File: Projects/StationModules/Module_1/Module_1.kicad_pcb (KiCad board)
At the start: 2 copper layers, 120 parts, among them J2 +310, J3 -310, J4 PowerTrans1, J5 PowerTrans2, M1 BluePillStm32, Q1 STD20NF06T4, Q2 STD20NF06T4, Q3 STD20NF06T4, Q4 STD20NF06T4, Q5 IRGB10B60KD, Q6 IRGB10B60KD, Q7 IRGB10B60KD, Q8 IRGB10B60KD, T1 Transformer_SP_2S, T2 Transformer_SP_2S, U1 PC817, U2 L7805, U3 TC1047AxNB, U5 LM311, U6 6N137

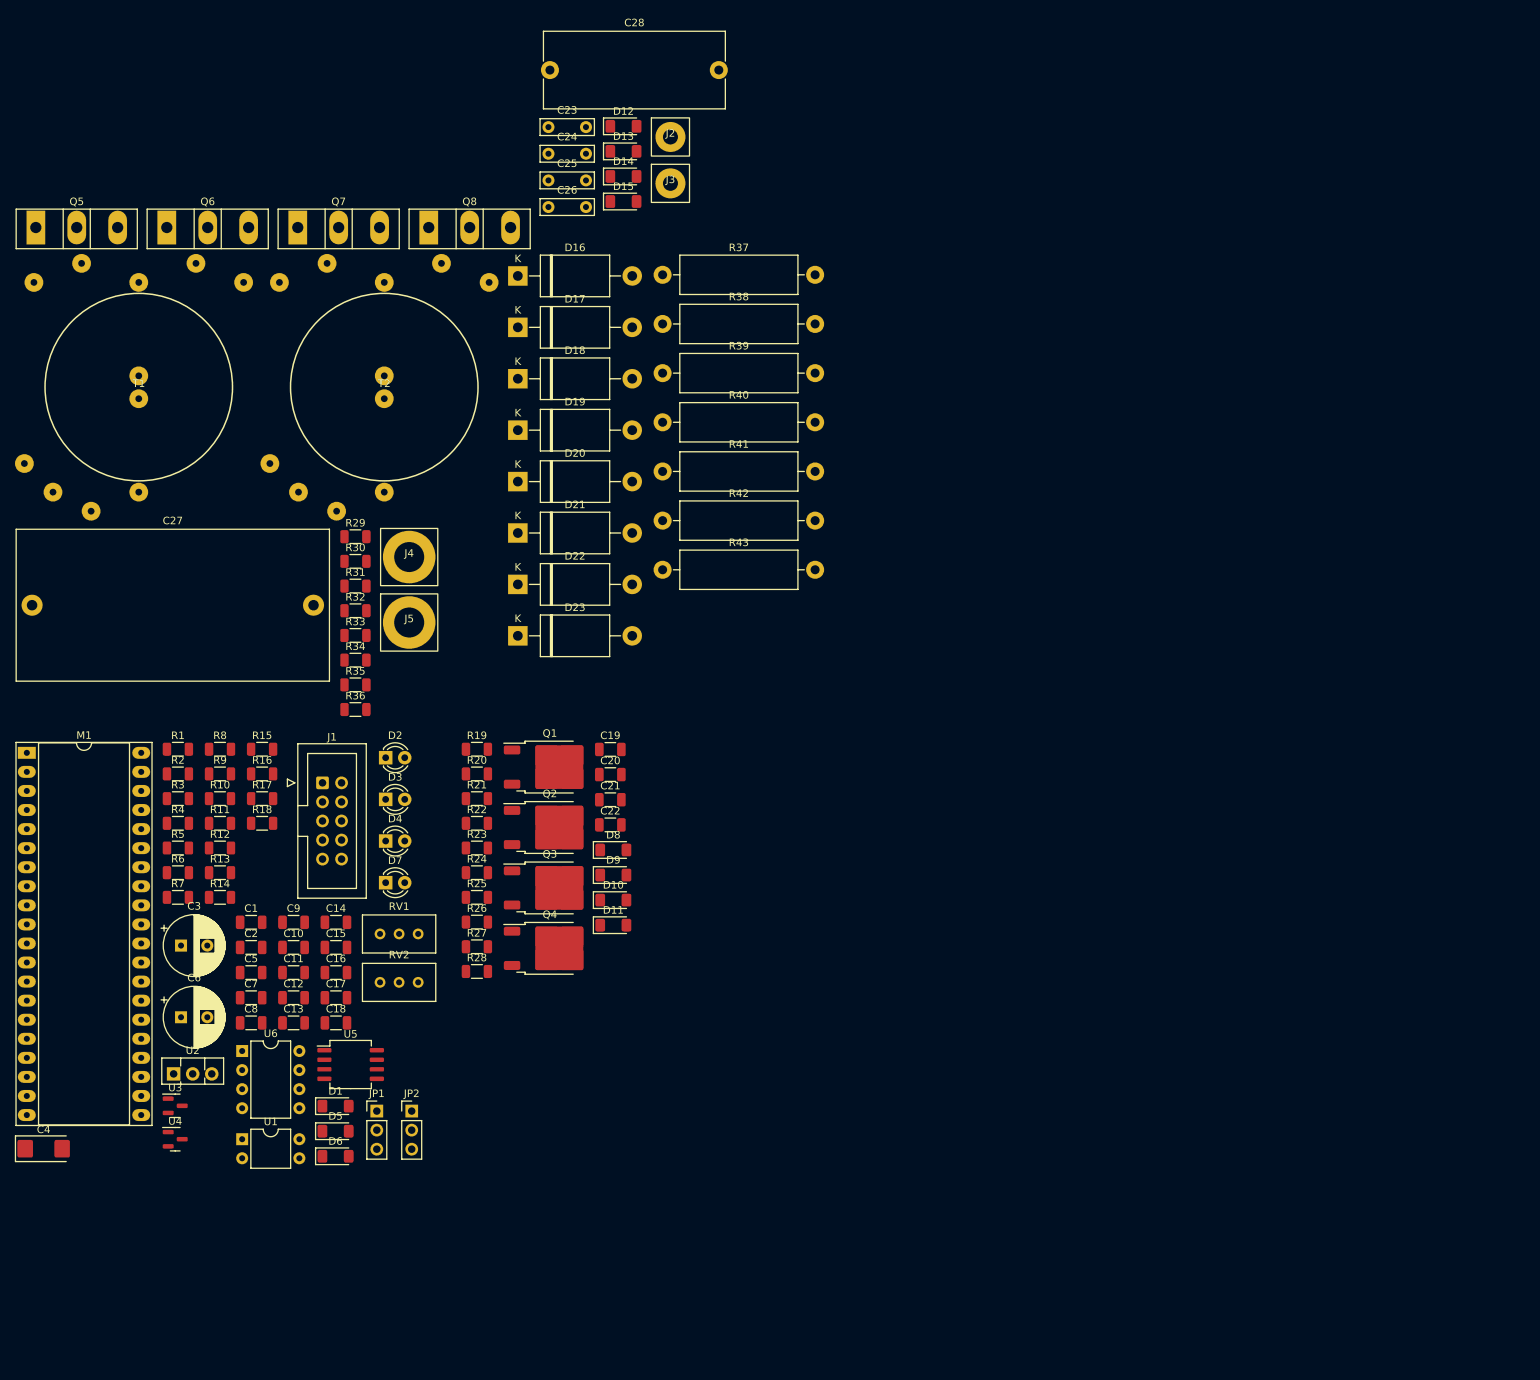
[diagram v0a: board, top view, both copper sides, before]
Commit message: Place elements 1
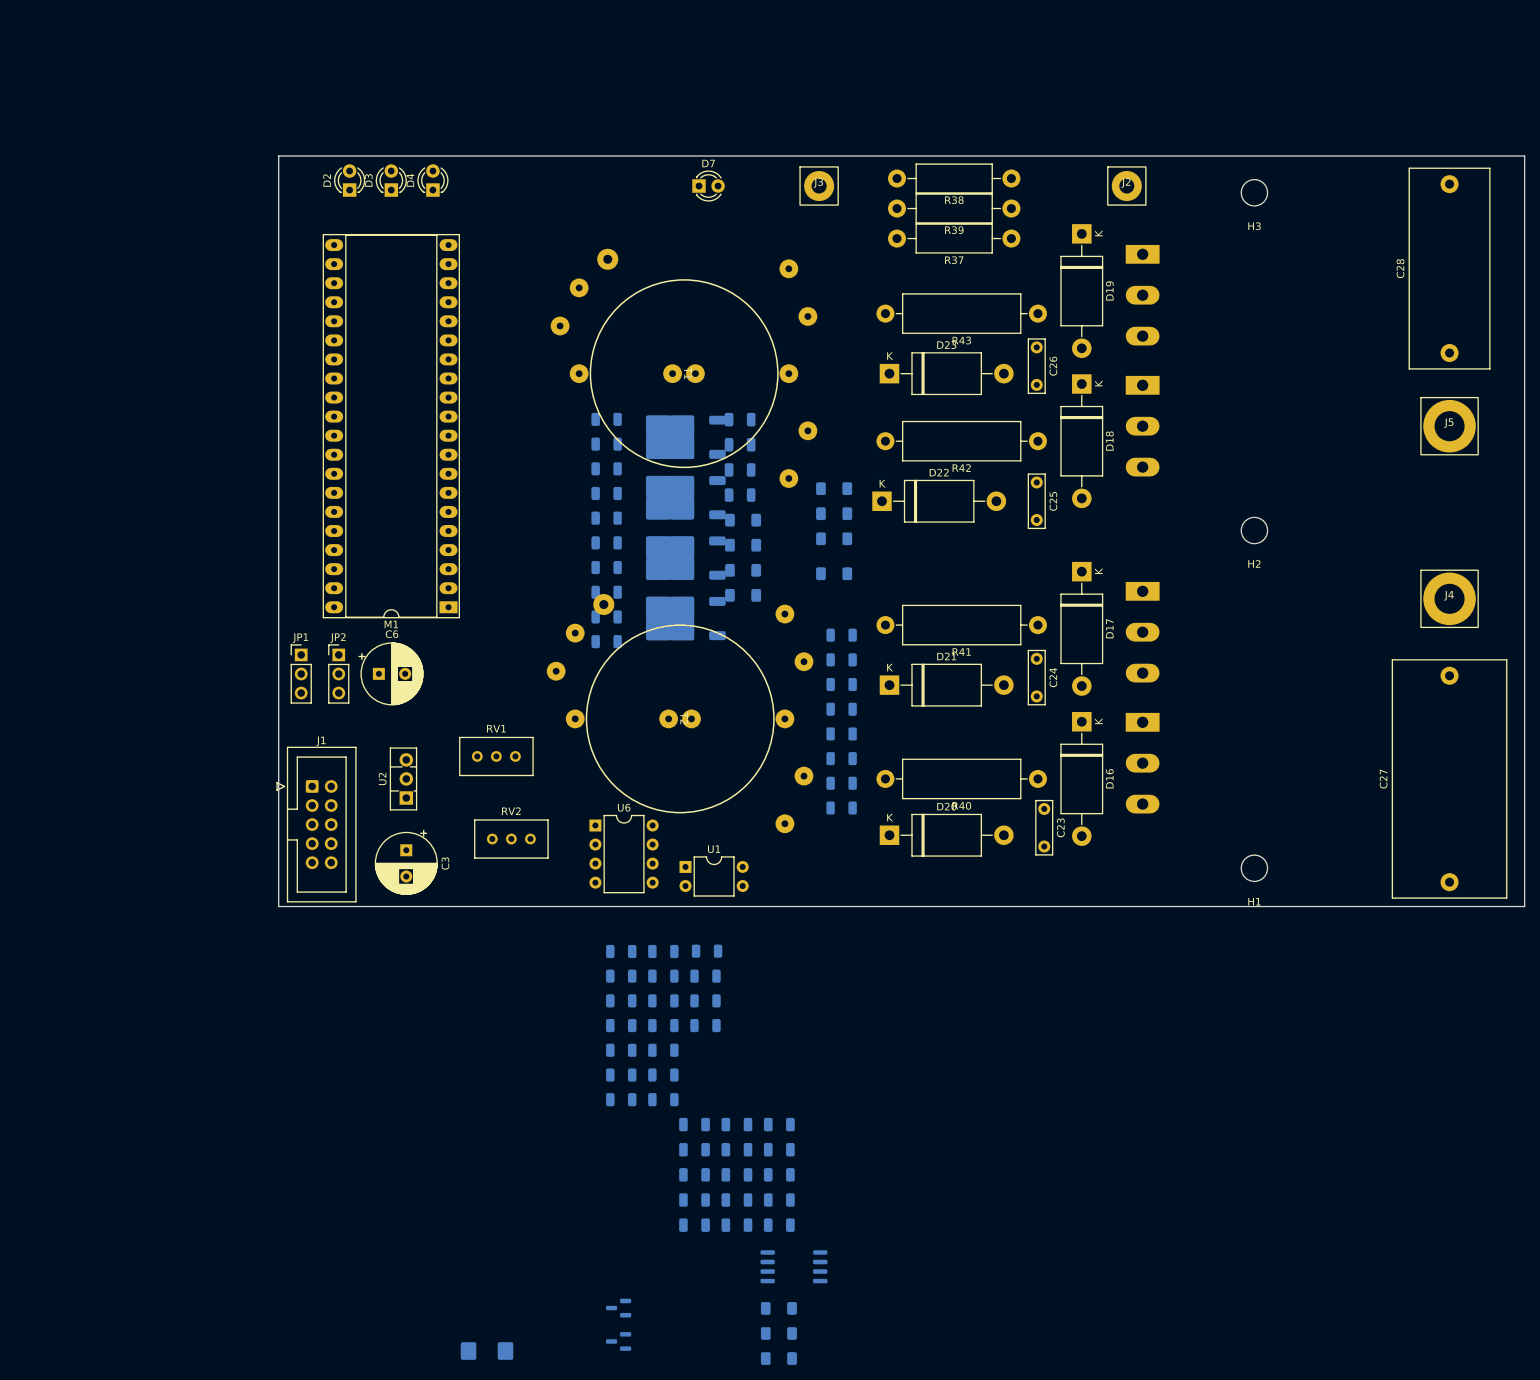
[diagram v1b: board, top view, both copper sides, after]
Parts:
- added H1: MountingHole, MountingHole:MountingHole_3.5mm, F.Cu at (184.0, 130.9)
- added H2: MountingHole, MountingHole:MountingHole_3.5mm, F.Cu at (184.0, 85.9)
- added H3: MountingHole, MountingHole:MountingHole_3.5mm, F.Cu at (184.0, 40.9)
- C1, C10, C11, C12, C13, C14, C15, C16, C17, C18, C19, C2, C20, C21, C22, C4, C5, C7, C8, C9, D1, D10, D11, D12, D13, D14, D15, D5, D6, D8, D9, Q1, Q2, Q3, Q4, R1, R10, R11, R12, R13, R14, R15, R16, R17, R18, R19, R2, R20, R21, R22, R23, R24, R25, R26, R27, R28, R29, R3, R30, R31, R32, R33, R34, R35, R36, R4, R5, R6, R7, R8, R9, U3, U4, U5: moved to B.Cu
- C27: footprint Capacitor_THT:C_Rect_L41.5mm_W20.0mm_P37.50mm_MKS4 -> Capacitor_THT:C_Rect_L31.5mm_W15.0mm_P27.50mm_MKS4
- C28: footprint Capacitor_THT:C_Rect_L24.0mm_W10.1mm_P22.50mm_MKT -> Capacitor_THT:C_Rect_L26.5mm_W10.5mm_P22.50mm_MKS4
- Q5, Q6, Q7, Q8: footprint Package_TO_SOT_THT:TO-247-3_Vertical -> Z_Package_TO:TO-247-3_Horizontal_TabUp; moved to B.Cu
- R37, R38, R39: footprint Resistor_THT:R_Axial_DIN0516_L15.5mm_D5.0mm_P20.32mm_Horizontal -> Resistor_THT:R_Axial_DIN0411_L9.9mm_D3.6mm_P15.24mm_Horizontal
- moved C27 192.4 mm to (210.0, 132.8), turned to 90 degrees
- moved Q5 161.5 mm to (169.1, 111.5), turned to -90 degrees
- moved J5 141.1 mm to (210.0, 72.0)
- moved Q6 138.8 mm to (169.1, 94.0), turned to -90 degrees
- moved J4 138.7 mm to (210.0, 95.0)
- moved C28 125.6 mm to (210.0, 62.2), turned to 90 degrees
- moved Q7 114.5 mm to (169.1, 66.5), turned to -90 degrees
- moved C23 112.3 mm to (156.0, 123.0), turned to -90 degrees
- moved D7 101.8 mm to (110.0, 40.0)
- moved D16 95.8 mm to (161.0, 111.4), turned to -90 degrees
- moved Q8 95.2 mm to (169.1, 49.1), turned to -90 degrees
- moved C24 93.6 mm to (155.0, 103.0), turned to -90 degrees
- moved D4 87.0 mm to (74.5, 40.5), turned to 90 degrees
- moved D17 81.9 mm to (161.0, 91.4), turned to -90 degrees
- moved D3 81.2 mm to (69.0, 40.5), turned to 90 degrees
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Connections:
- C24 pad 1: Net-(D16-A1) -> Net-(D16-A2)
- C26 pad 1: Net-(D18-A1) -> Net-(D18-A2)
- C27 pad 1: Net-(D16-A1) -> Net-(D16-A2)
- D16 pad 1: Net-(D16-A1) -> Net-(D14-A)
- D16 pad 2: Net-(D14-A) -> Net-(D16-A2)
- D17 pad 1: /Shunt+ -> Net-(D15-A)
- D17 pad 2: Net-(D15-A) -> /Shunt+
- D18 pad 1: Net-(D18-A1) -> Net-(D12-A)
- D18 pad 2: Net-(D12-A) -> Net-(D18-A2)
- D19 pad 1: /Shunt+ -> Net-(D13-A)
- D19 pad 2: Net-(D13-A) -> /Shunt+
- D20 pad 1: Net-(D16-A1) -> Net-(D16-A2)
- D22 pad 1: Net-(D18-A1) -> Net-(D18-A2)
- J5 pad 1: Net-(D18-A1) -> Net-(D18-A2)
- Q5 pad 3: Net-(D16-A1) -> Net-(D16-A2)
- Q6 pad 2: Net-(D16-A1) -> Net-(D16-A2)
- Q7 pad 3: Net-(D18-A1) -> Net-(D18-A2)
- Q8 pad 2: Net-(D18-A1) -> Net-(D18-A2)
- R33 pad 1: Net-(D16-A1) -> Net-(D16-A2)
- R35 pad 1: Net-(D18-A1) -> Net-(D18-A2)
- R40 pad 2: Net-(D16-A1) -> Net-(D16-A2)
- R42 pad 2: Net-(D18-A1) -> Net-(D18-A2)
- T1 pad 5: Net-(D16-A1) -> Net-(D16-A2)
- T2 pad 5: Net-(D18-A1) -> Net-(D18-A2)
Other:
- board outline added: 166 x 100 mm

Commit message: Place elements 2
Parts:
- moved U3 152.5 mm to (162.6, 50.8)
- moved C12 136.0 mm to (162.6, 47.6), turned to 0 degrees
- moved R7 125.6 mm to (78.5, 37.9), turned to 0 degrees
- moved C1 122.8 mm to (78.5, 46.2)
- moved C2 121.2 mm to (78.5, 51.2)
- moved R6 120.1 mm to (78.5, 40.2), turned to 0 degrees
- moved R5 114.9 mm to (78.5, 42.2), turned to 0 degrees
- moved C4 109.1 mm to (103.5, 88.3), turned to 90 degrees
- moved R9 107.8 mm to (162.6, 54.0)
- moved C11 101.4 mm to (73.7, 79.2), turned to 0 degrees
- moved D1 95.4 mm to (82.5, 102.0), turned to -90 degrees
- moved D7 95.0 mm to (123.8, 134.0), turned to 90 degrees
- moved J3 93.6 mm to (137.0, 133.0)
- moved C10 90.4 mm to (73.7, 88.1), turned to 0 degrees
- moved R37 87.7 mm to (163.0, 134.0)
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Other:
- board size 166 x 100 mm -> 155 x 100 mm

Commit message: Trace complit 1
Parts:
- added ?: , , F.Cu at (206.0, 41.7)
- added C29: 0,1uF, Capacitor_SMD:C_1206_3216Metric, B.Cu at (151.6, 39.9)
- moved C19 42.1 mm to (105.9, 44.2)
- moved D2 38.8 mm to (64.0, 72.4), turned to -90 degrees
- moved D3 35.4 mm to (64.0, 63.0), turned to -90 degrees
- moved D4 35.1 mm to (64.0, 53.3), turned to -90 degrees
- moved R27 30.0 mm to (117.6, 54.6), turned to 90 degrees
- moved R5 30.0 mm to (65.0, 68.9), turned to -90 degrees
- moved J2 28.0 mm to (157.0, 85.3)
- moved D8 27.9 mm to (102.1, 55.9), turned to 0 degrees
- moved R19 26.2 mm to (102.1, 52.3), turned to -90 degrees
- moved R36 26.1 mm to (125.2, 121.0), turned to 90 degrees
- moved R13 25.1 mm to (103.4, 134.6), turned to 180 degrees
- moved D11 24.9 mm to (102.1, 106.2), turned to 0 degrees
- moved R41 24.5 mm to (135.4, 75.9), turned to 0 degrees
- moved R42 23.9 mm to (136.1, 103.6), turned to 0 degrees
- moved R6 23.6 mm to (65.0, 59.5), turned to -90 degrees
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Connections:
- C1 pad 1: +3.3V -> +3V3
- M1 pad 20: +3.3V -> +3V3
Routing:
- net +5V: track 0.00 -> 203.9 mm, vias 0 -> 1
- net /Shunt+: track 0.00 -> 188.1 mm, vias 0 -> 1
- net +12V: track 0.00 -> 181.7 mm, vias 0 -> 3
- net /TMP: track 0.00 -> 126.4 mm
- net /Shunt-: track 0.00 -> 115.0 mm
- net Net-(J2-Pin_1): track 0.00 -> 109.0 mm
- net Net-(D16-A2): track 0.00 -> 85.7 mm
- net Net-(D18-A2): track 0.00 -> 81.3 mm
- net +3V3: track 0.00 -> 72.9 mm
- net /IN_1: track 0.00 -> 61.2 mm, vias 0 -> 1
- net Net-(D13-A): track 0.00 -> 60.4 mm, vias 0 -> 1
- net GND: track 0.00 -> 60.1 mm, vias 0 -> 56
- net Net-(D15-A): track 0.00 -> 59.8 mm, vias 0 -> 1
- net Net-(D14-A): track 0.00 -> 58.9 mm, vias 0 -> 1
- net Net-(D12-A): track 0.00 -> 54.8 mm, vias 0 -> 1
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- added copper zone on B.Cu, net /Shunt+
- added copper zone on B.Cu, net /Shunt-
- added copper zone on B.Cu, net GND
- added copper zone on F.Cu, net GND
- added copper zone on B.Cu, net Net-(D16-A2)
- added copper zone on B.Cu, net Net-(D18-A2)
- added copper zone on B.Cu, net Net-(J4-Pin_1)
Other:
- board size 155 x 100 mm -> 156 x 101.5 mm

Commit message: Trace complit 2
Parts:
- U5: footprint Package_SO:SO-8_5.3x6.2mm_P1.27mm -> Package_SO:SO-8_3.9x4.9mm_P1.27mm
- moved D2 39.0 mm to (85.1, 39.6), turned to 90 degrees
- moved R5 32.5 mm to (79.2, 39.6), turned to 0 degrees
- moved D3 23.6 mm to (67.6, 39.6), turned to 90 degrees
- moved R6 22.0 mm to (71.9, 38.6), turned to 90 degrees
- moved D4 13.7 mm to (63.0, 39.6), turned to 90 degrees
- moved R32 7.62 mm to (128.3, 70.9), turned to 90 degrees
- moved R7 6.24 mm to (63.0, 43.9)
- moved C6 3.69 mm to (92.7, 44.4)
- moved R40 3.30 mm to (132.3, 57.4)
- moved R41 3.05 mm to (132.3, 75.9)
- moved D19 1.34 mm to (164.3, 110.5)
- moved D16 1.27 mm to (164.3, 45.2)
- moved D17 1.27 mm to (164.3, 65.5)
- moved D18 1.27 mm to (164.3, 89.4)
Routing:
- net /LED3: track 7.65 -> 27.1 mm
- net /LED2: track 3.57 -> 21.4 mm
- net /LED1: track 6.79 -> 14.7 mm
- net Net-(J2-Pin_1): track 109.0 -> 104.8 mm
- net Net-(D15-A): track 59.8 -> 63.9 mm, vias 1 -> 0
- net Net-(D4-A): track 6.67 -> 2.85 mm
- net /TMP: track 126.4 -> 123.1 mm
- net Net-(D21-A2): track 17.9 -> 21.0 mm
- net Net-(D20-A2): track 13.0 -> 16.0 mm
- net Net-(D3-A): track 2.45 -> 5.35 mm
- net Net-(D16-A2): track 85.7 -> 83.2 mm
- net Net-(D2-A): track 2.45 -> 4.38 mm
- net /Shunt+: track 188.1 -> 190.0 mm
- net +5V: track 203.9 -> 205.6 mm
- net Net-(U5--): track 10.6 -> 11.8 mm
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
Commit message: Trace complit 3
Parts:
- moved C29 20.3 mm to (171.9, 39.1)
- moved U3 19.6 mm to (175.7, 40.6), turned to -90 degrees
- moved R9 16.0 mm to (175.5, 37.6), turned to 180 degrees
- moved C12 14.2 mm to (168.8, 37.8)
- moved R37 0.37 mm to (158.5, 134.4)
- moved R38 0.25 mm to (158.5, 125.7)
- gave numbers to parts that had none: 1
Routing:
- net GND: track 60.1 -> 78.2 mm
- net /TMP: track 123.1 -> 138.9 mm
- net +5V: track 205.6 -> 221.4 mm
- net Net-(U3-V_{OUT}): track 4.55 -> 2.24 mm
- net Net-(D16-A2): track 83.2 -> 82.0 mm
- net Net-(D14-A): track 58.9 -> 57.8 mm
- net /Shunt-: track 115.4 -> 114.5 mm

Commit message: Prod complit 1
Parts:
- added ?: , , F.Cu at (104.4, 42.7)
- added ?: , , F.Cu at (104.1, 94.0)
- moved C20 4.32 mm to (108.2, 91.4)
- moved C19 3.35 mm to (109.0, 42.9)
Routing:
- net +12V: track 181.7 -> 189.1 mm
- net GND: track 78.2 -> 72.4 mm, vias 69 -> 70
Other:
- board text added: "1"
- board text added: "2"
- board text added: "3"
- board text added: "4"
- board text added: "5"
- board text added: "6"
- board text added: "7"

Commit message: add bom module 1
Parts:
- added C30: 0,1uF, Capacitor_SMD:C_1206_3216Metric, B.Cu at (63.8, 78.2)
- added D24: SMBJ18CA, Diode_SMD:D_SMB, F.Cu at (164.3, 119.0)
- added D25: SMBJ18CA, Diode_SMD:D_SMB, F.Cu at (164.3, 97.8)
- added D26: SMBJ18CA, Diode_SMD:D_SMB, F.Cu at (164.3, 74.2)
- added D27: SMBJ18CA, Diode_SMD:D_SMB, F.Cu at (155.7, 51.7)
- added D28: ES3JC, Diode_SMD:D_SMC, B.Cu at (143.3, 51.8)
- added D29: ES3JC, Diode_SMD:D_SMC, B.Cu at (143.7, 72.9)
- added D30: ES3JC, Diode_SMD:D_SMC, B.Cu at (144.7, 98.3)
- added D31: ES3JC, Diode_SMD:D_SMC, B.Cu at (144.8, 116.6)
- added R44: 0,01, Resistor_SMD:R_2816_7142Metric, B.Cu at (150.6, 134.1)
- added R45: 0,01, Resistor_SMD:R_2816_7142Metric, B.Cu at (150.6, 129.0)
- added R46: 0,01, Resistor_SMD:R_2816_7142Metric, B.Cu at (150.6, 124.0)
- C4: footprint Capacitor_Tantalum_SMD:CP_EIA-6032-28_Kemet-C -> Capacitor_Tantalum_SMD:CP_EIA-7343-15_Kemet-W
- R37, R38, R39: value 0,1 -> 0,01
- moved C4 0.06 mm to (109.3, 76.7)
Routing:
- net /Shunt+: track 190.0 -> 204.1 mm
- net Net-(D14-A): track 57.8 -> 68.3 mm
- net Net-(D16-A2): track 82.0 -> 91.4 mm
- net Net-(D18-A2): track 81.3 -> 89.6 mm
- net Net-(D22-A2): track 18.5 -> 25.9 mm
- net Net-(D15-A): track 63.7 -> 70.2 mm
- net Net-(D13-A): track 60.4 -> 66.8 mm
- net Net-(D12-A): track 54.8 -> 61.1 mm
- net Net-(D20-A2): track 16.0 -> 20.3 mm
- net Net-(D21-A2): track 21.0 -> 24.1 mm
- net Net-(D23-A2): track 18.7 -> 20.6 mm
- net /OS: track 30.0 -> 31.7 mm
- net +12V: track 189.1 -> 188.6 mm
